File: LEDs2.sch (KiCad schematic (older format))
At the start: 116 parts

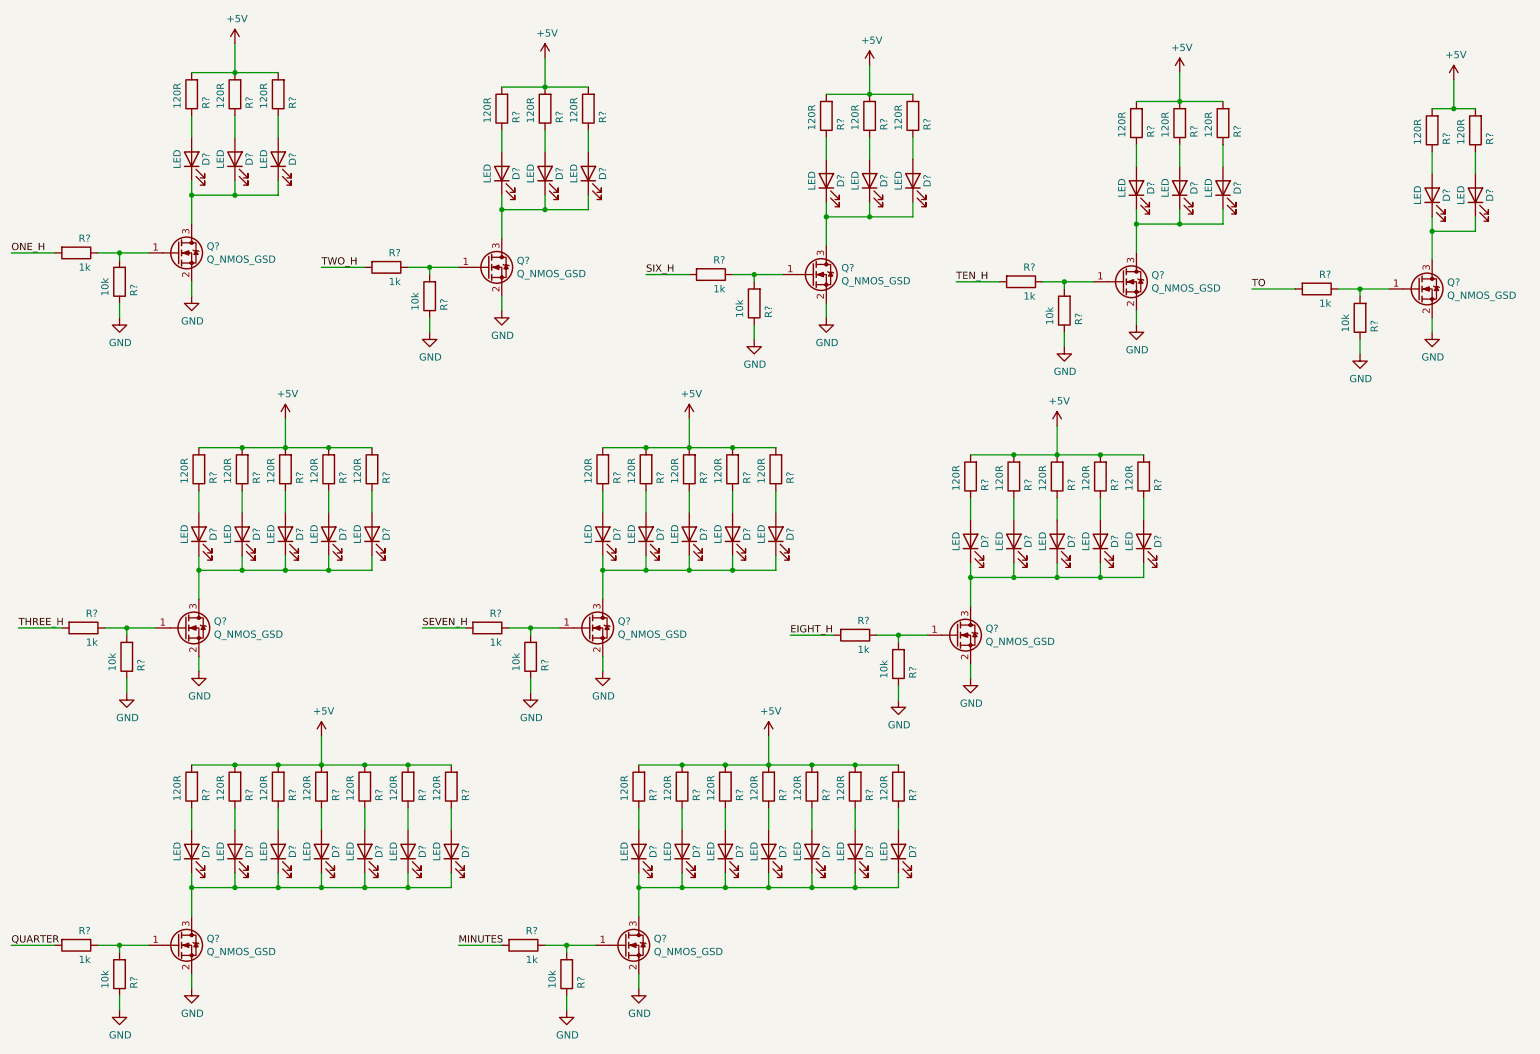
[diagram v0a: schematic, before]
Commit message: Schematic is almost finished. The MCLR circuit needs completing, the hour/minute inputs also need their input protection.
After that, I might have one of the guys from work review it. But, who knows.
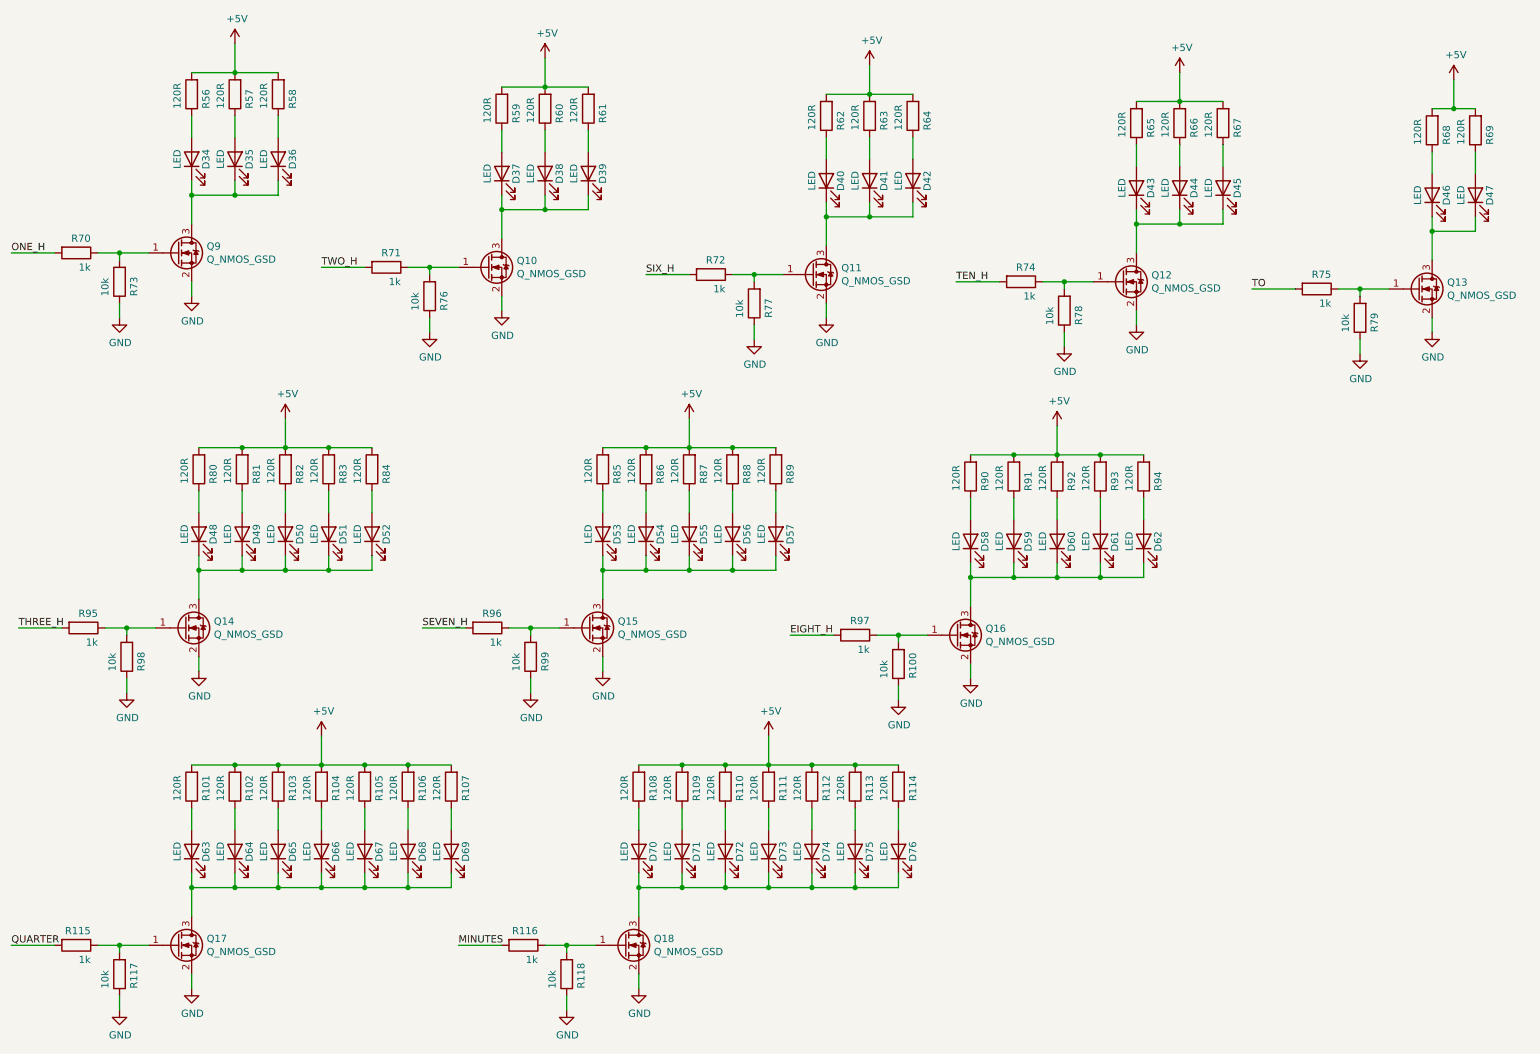
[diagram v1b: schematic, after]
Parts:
- gave numbers to parts that had none: 116
